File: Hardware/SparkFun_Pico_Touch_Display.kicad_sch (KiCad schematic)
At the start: 53 parts, among them J1 Conn_01x20, J2 Conn_01x20, J3 Conn_02x10_SMD_RA, J4 Conn_1x21_FPC, J5 Qwiic_Vertical, J6 microSD, Q1 RE1C002UNTCL, SW1 SMD_4.6x2.8mm_h2.5mm, U1 2" LCD-TFT 240x320, U2 PCA9534PW

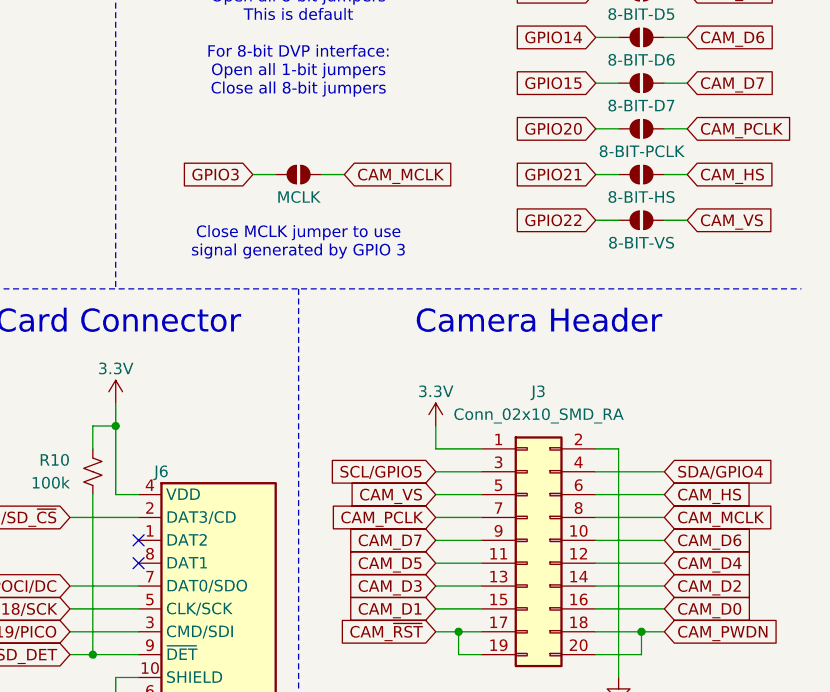
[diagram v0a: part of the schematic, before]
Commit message: Rename MCLK to XCLK
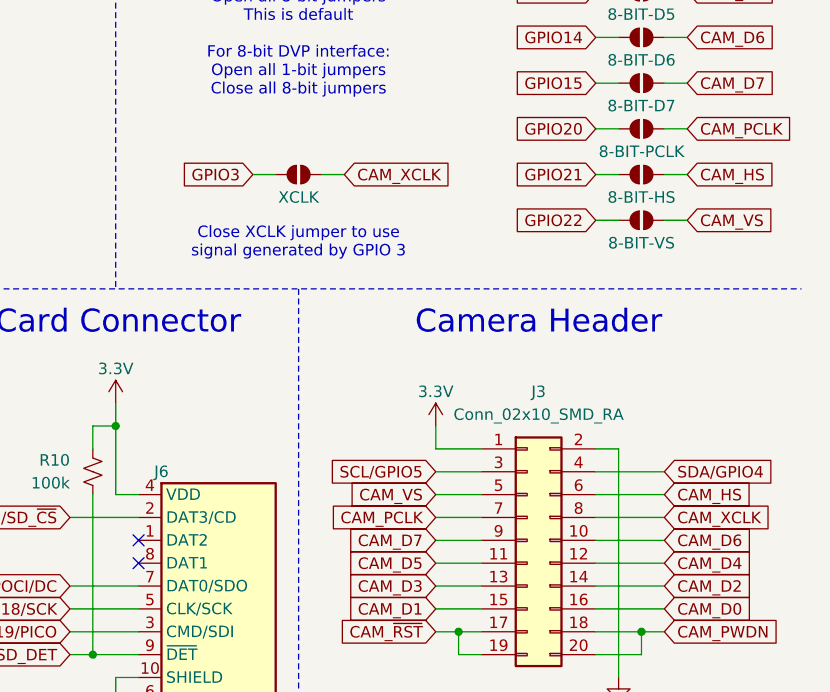
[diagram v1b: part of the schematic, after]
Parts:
- JP13: value MCLK -> XCLK
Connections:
- net CAM_MCLK renamed CAM_XCLK
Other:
- note added: "Close XCLK jumper to use signal generated by GPIO 3"
- note removed: "Close MCLK jumper to use signal generated by GPIO 3"
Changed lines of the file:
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@@
 		)
 	)
-	(text "Close MCLK jumper to use\nsignal generated by GPIO 3"
+	(text "Close XCLK jumper to use\nsignal generated by GPIO 3"
 		(exclude_from_sim no)
 		(at 210.82 86.36 0)
@@
 		)
 	)
-	(global_label "CAM_MCLK"
+	(global_label "CAM_XCLK"
 		(shape input)
 		(at 251.46 116.84 0)
@@
 		)
 	)
-	(global_label "CAM_MCLK"
+	(global_label "CAM_XCLK"
 		(shape input)
 		(at 215.9 78.74 0)
@@
 			)
 		)
-		(property "Value" "MCLK"
+		(property "Value" "XCLK"
 			(at 210.82 81.28 0)
 			(effects

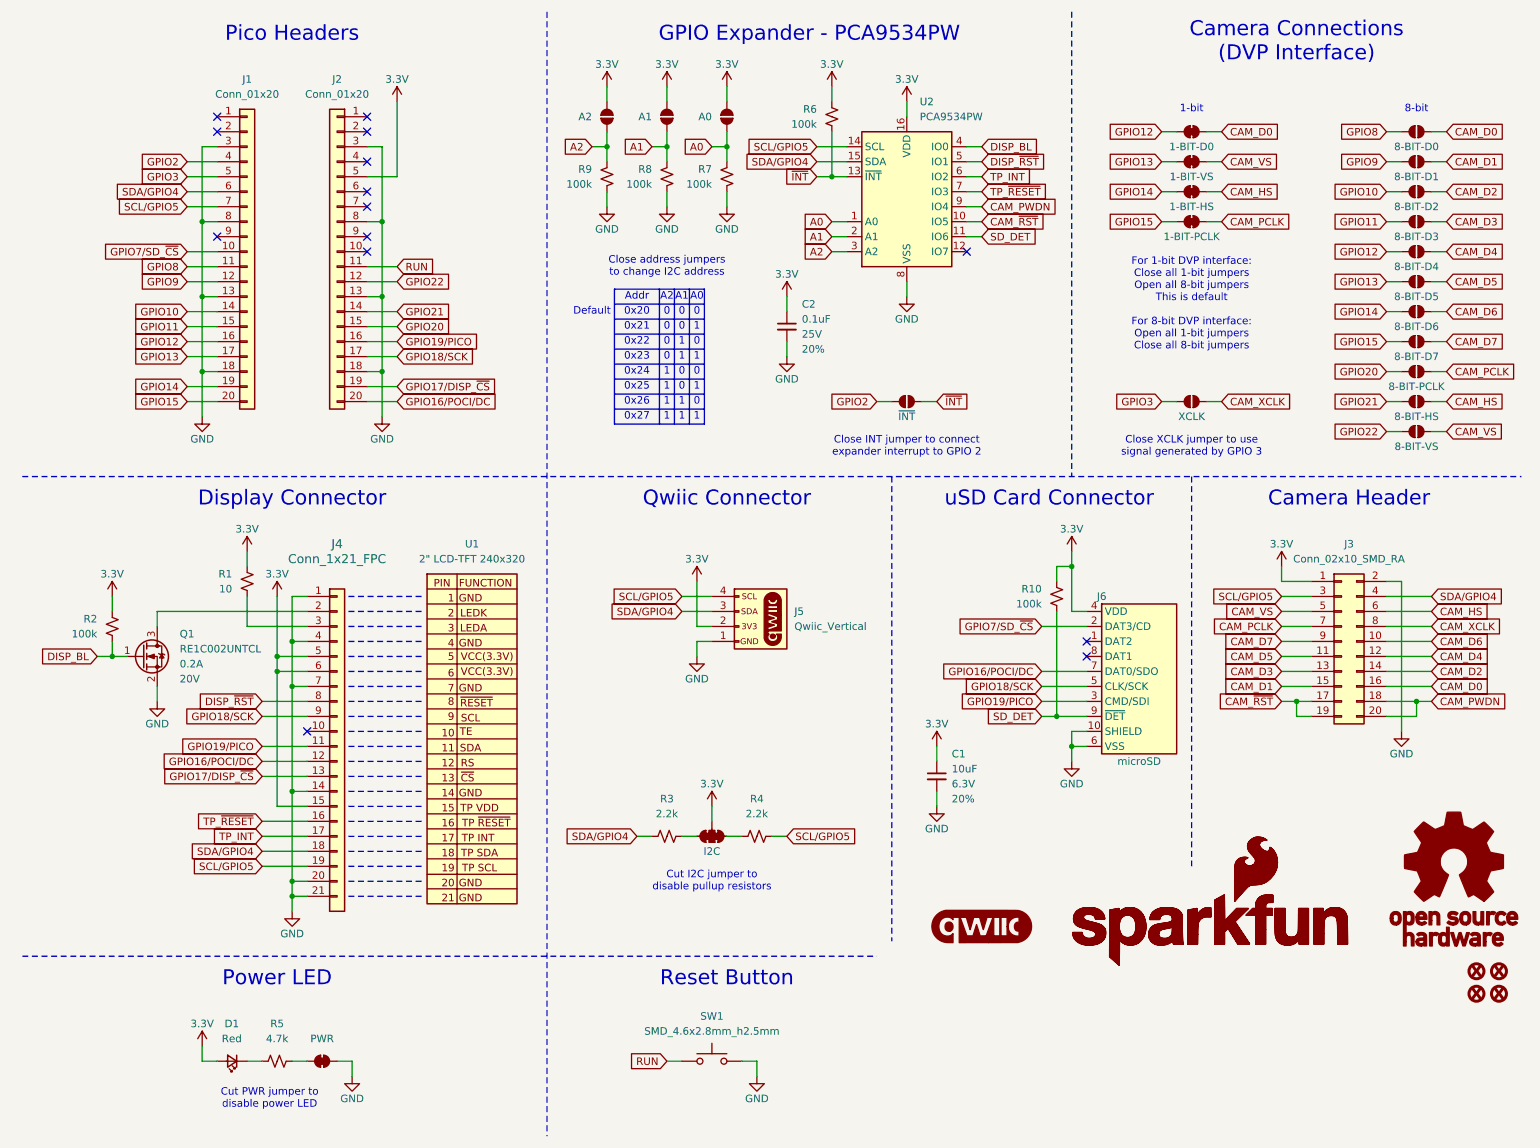
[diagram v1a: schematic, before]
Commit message: Add pullup resistors to TP and DISP RST nets
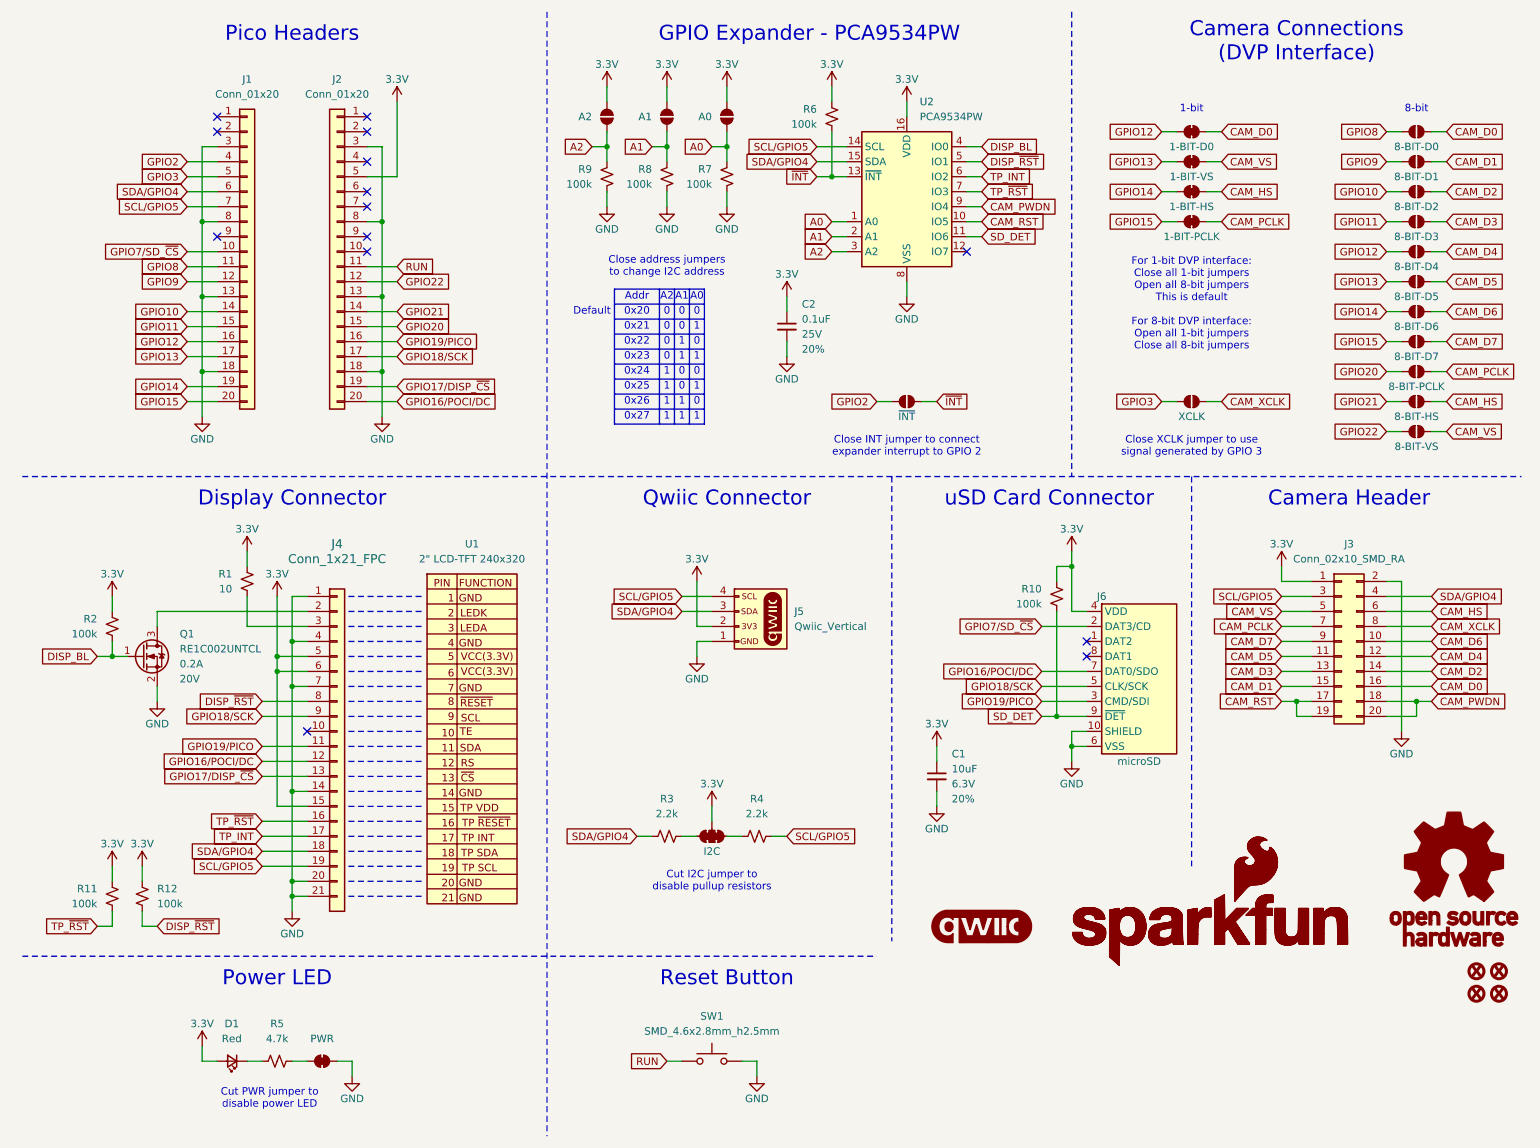
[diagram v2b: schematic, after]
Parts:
- added R11, R12: 100k, SparkFun-Resistor:R_0603_1608Metric, symbol SparkFun-Resistor:100k_0603
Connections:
- net 3.3V: now also R11.2, R12.2
- net DISP_~{RST}: now also R12.1
- net CAM_~{RST} renamed CAM_RST
- net TP_~{RESET} renamed TP_~{RST}
- net TP_~{RST}: now also R11.1
